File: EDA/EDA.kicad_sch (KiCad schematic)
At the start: 38 parts, among them J2 Screw_Terminal_01x02, M1 Motor_Servo, U1 PMCF8316A1VRGFR, U2 LM2596S-5, U3 LM2678S-5.0

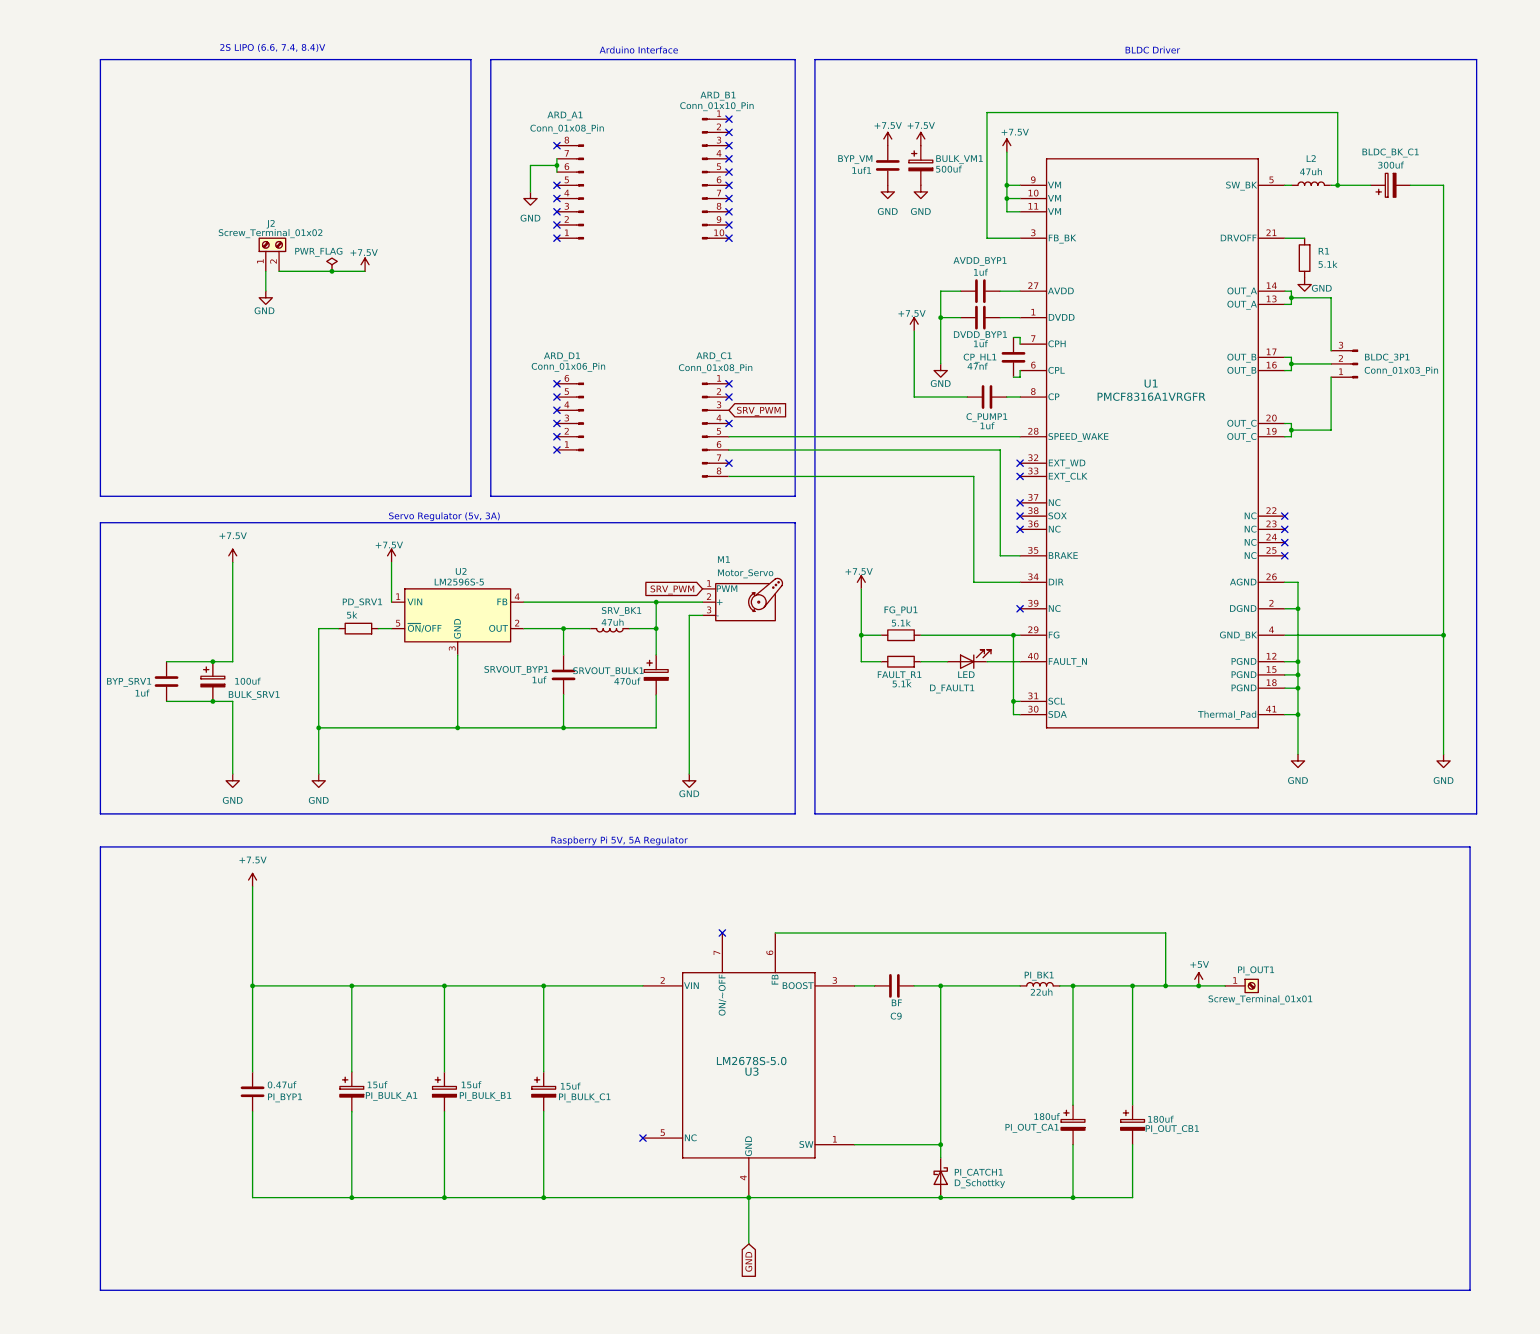
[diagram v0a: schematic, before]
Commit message: Add No-Connect flags and add labels, create ground terminal for Raspberry Pi.
Started Routing PCB.

- Developed Pi 5V, 5A power supply.
- Working on 5V, 3A servo power supply.
- Yet to begin wiring BLDC motor controller logic.
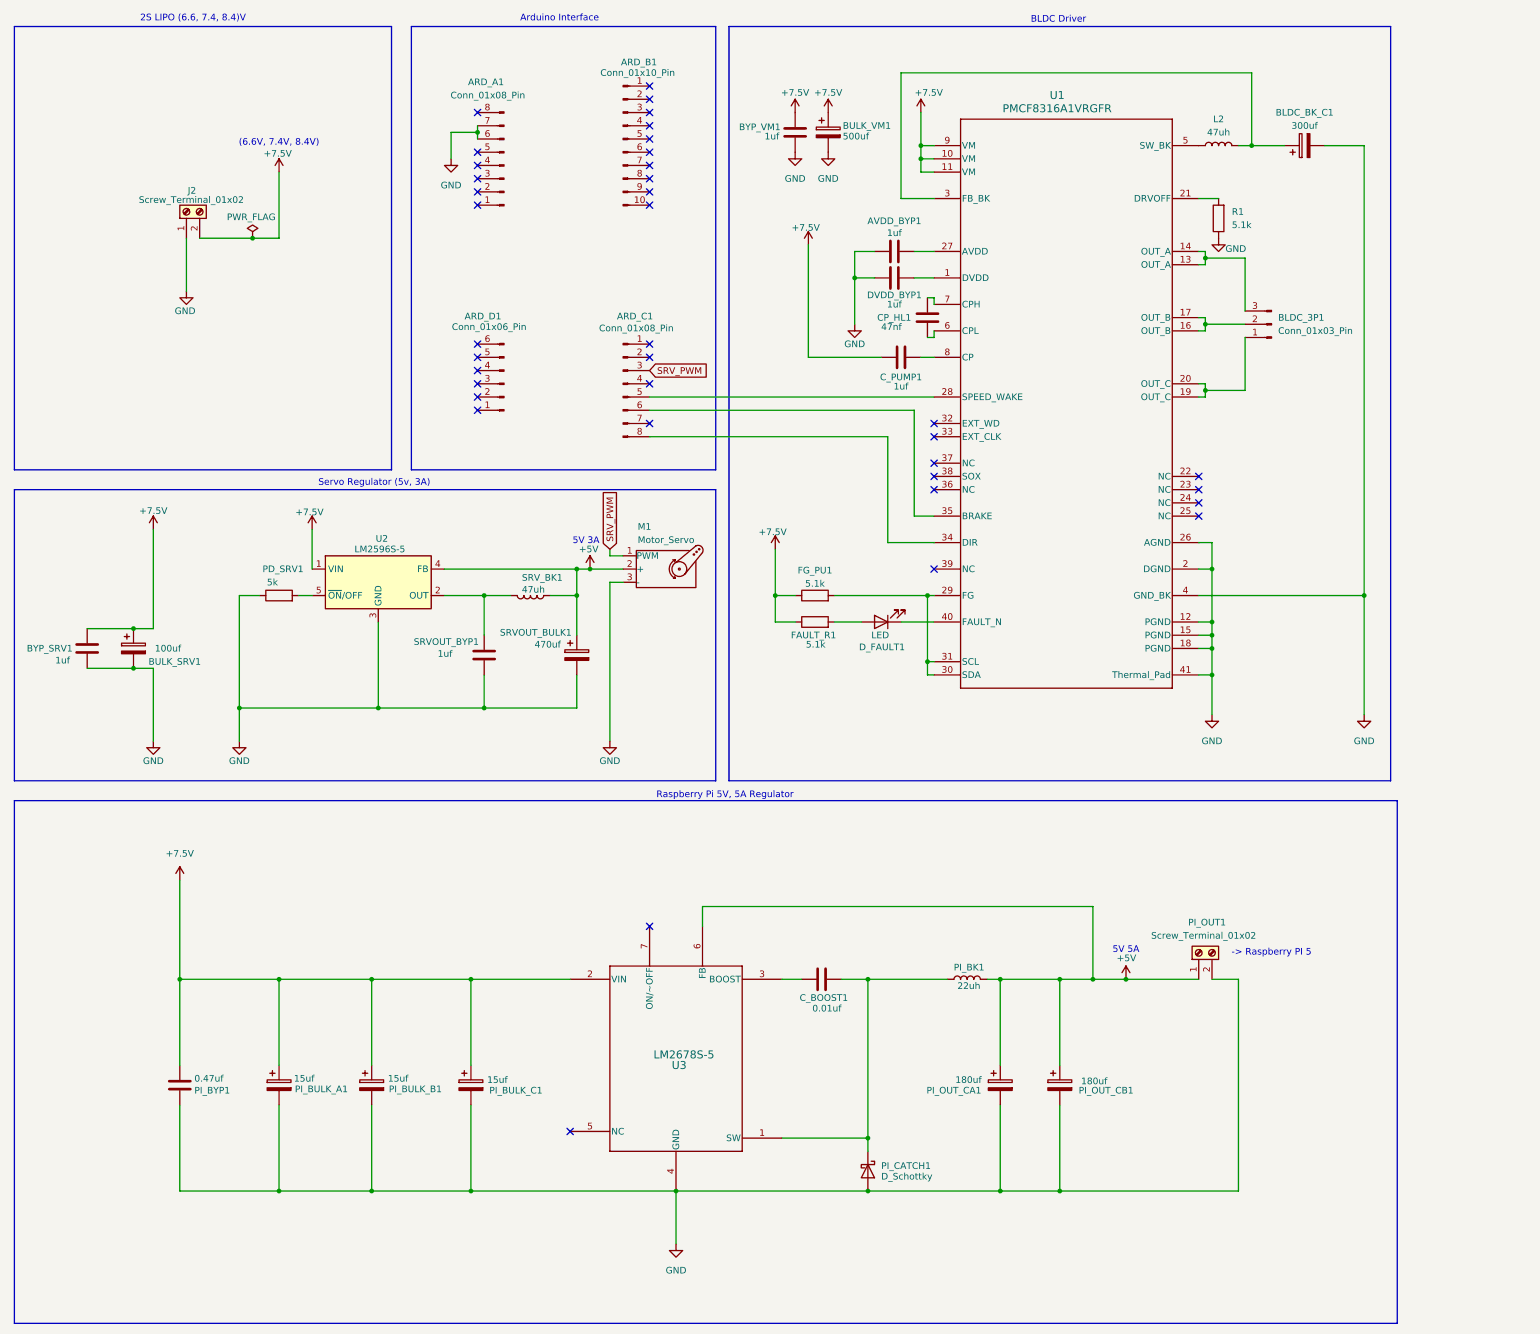
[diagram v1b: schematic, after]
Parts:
- removed PI_OUT1: Screw_Terminal_01x01, symbol Connector:Screw_Terminal_01x01
- added PI_OUT1: Screw_Terminal_01x02, Connector_Wire:SolderWire-1.5sqmm_1x02_P7.8mm_D1.7mm_OD3.9mm, symbol Connector:Screw_Terminal_01x02
- BLDC_BK_C1: footprint (none) -> Capacitor_THT:CP_Radial_D8.0mm_P3.50mm
- BULK_SRV1, PI_BULK_A1, PI_BULK_B1, PI_BULK_C1: footprint (none) -> Capacitor_THT:CP_Radial_D7.5mm_P2.50mm
- BYP_SRV1, PI_BYP1: footprint (none) -> Capacitor_SMD:C_0402_1005Metric
- BYP_VM1: renamed from 1uf1; value BYP_VM -> 1uf
- C_BOOST1: renamed from C9; value BF -> 0.01uf; footprint (none) -> Capacitor_SMD:C_0402_1005Metric
- PI_BK1: footprint (none) -> Inductor_SMD:L_0201_0603Metric
- PI_CATCH1: footprint (none) -> Diode_SMD:D_0201_0603Metric
- PI_OUT_CA1, PI_OUT_CB1: footprint (none) -> Capacitor_THT:CP_Radial_D8.0mm_P2.50mm
- SRVOUT_BULK1: footprint (none) -> Capacitor_THT:CP_Radial_D8.0mm_P3.80mm
- SRVOUT_BYP1: footprint (none) -> Capacitor_SMD:C_0201_0603Metric
- U3: value LM2678S-5.0 -> LM2678S-5
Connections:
- net +5V: now also M1.2 (+), SRVOUT_BULK1.1, SRV_BK1.1, U2.4 (FB), PI_OUT1.1 (Pin_1)
- net GND: now also PI_OUT1.2 (Pin_2)
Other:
- note added: "(6.6V, 7.4V, 8.4V)"
- note added: "-> Raspberry PI 5"
- note added: "5V 3A"
- note added: "5V 5A"
- company: (none) -> Apostla
- title: (none) -> BLDC Driver + Servo Shield + 5V, 5A Supply
- moved on the sheet: ARD_A1, ARD_B1, ARD_C1, ARD_D1, AVDD_BYP1, BLDC_3P1, BLDC_BK_C1, BULK_SRV1, BULK_VM1, BYP_SRV1, BYP_VM1, CP_HL1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

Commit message: Add initial EDA project files and configuration
- Created EDA.step file for project steps.
- Added autosave configuration for EDA.kicad_prl with board settings, visibility options, and net inspector panel configurations.
- Introduced lock files for PCB and schematic with hostname and username information.

Add components table to README

Added a table listing various components with their products and prices.

Add new symbols and footprints for UCY2D181MHD3TN and VS-6TQ045S-M3 components

- Created symbol for UCY2D181MHD3TN with properties including reference, value, footprint, and datasheet.
- Added footprint for UCY2D181MHD3TN with dimensions and pad specifications.
- Created symbol for VS-6TQ045S-M3 with properties including reference, value, footprint, and datasheet link.
- Added multiple footprints for VS-6TQ045S-M3, including DPAK_045S-M3_VIS, DPAK_045S-M3_VIS-L, and DPAK_045S-M3_VIS-M with detailed specifications.
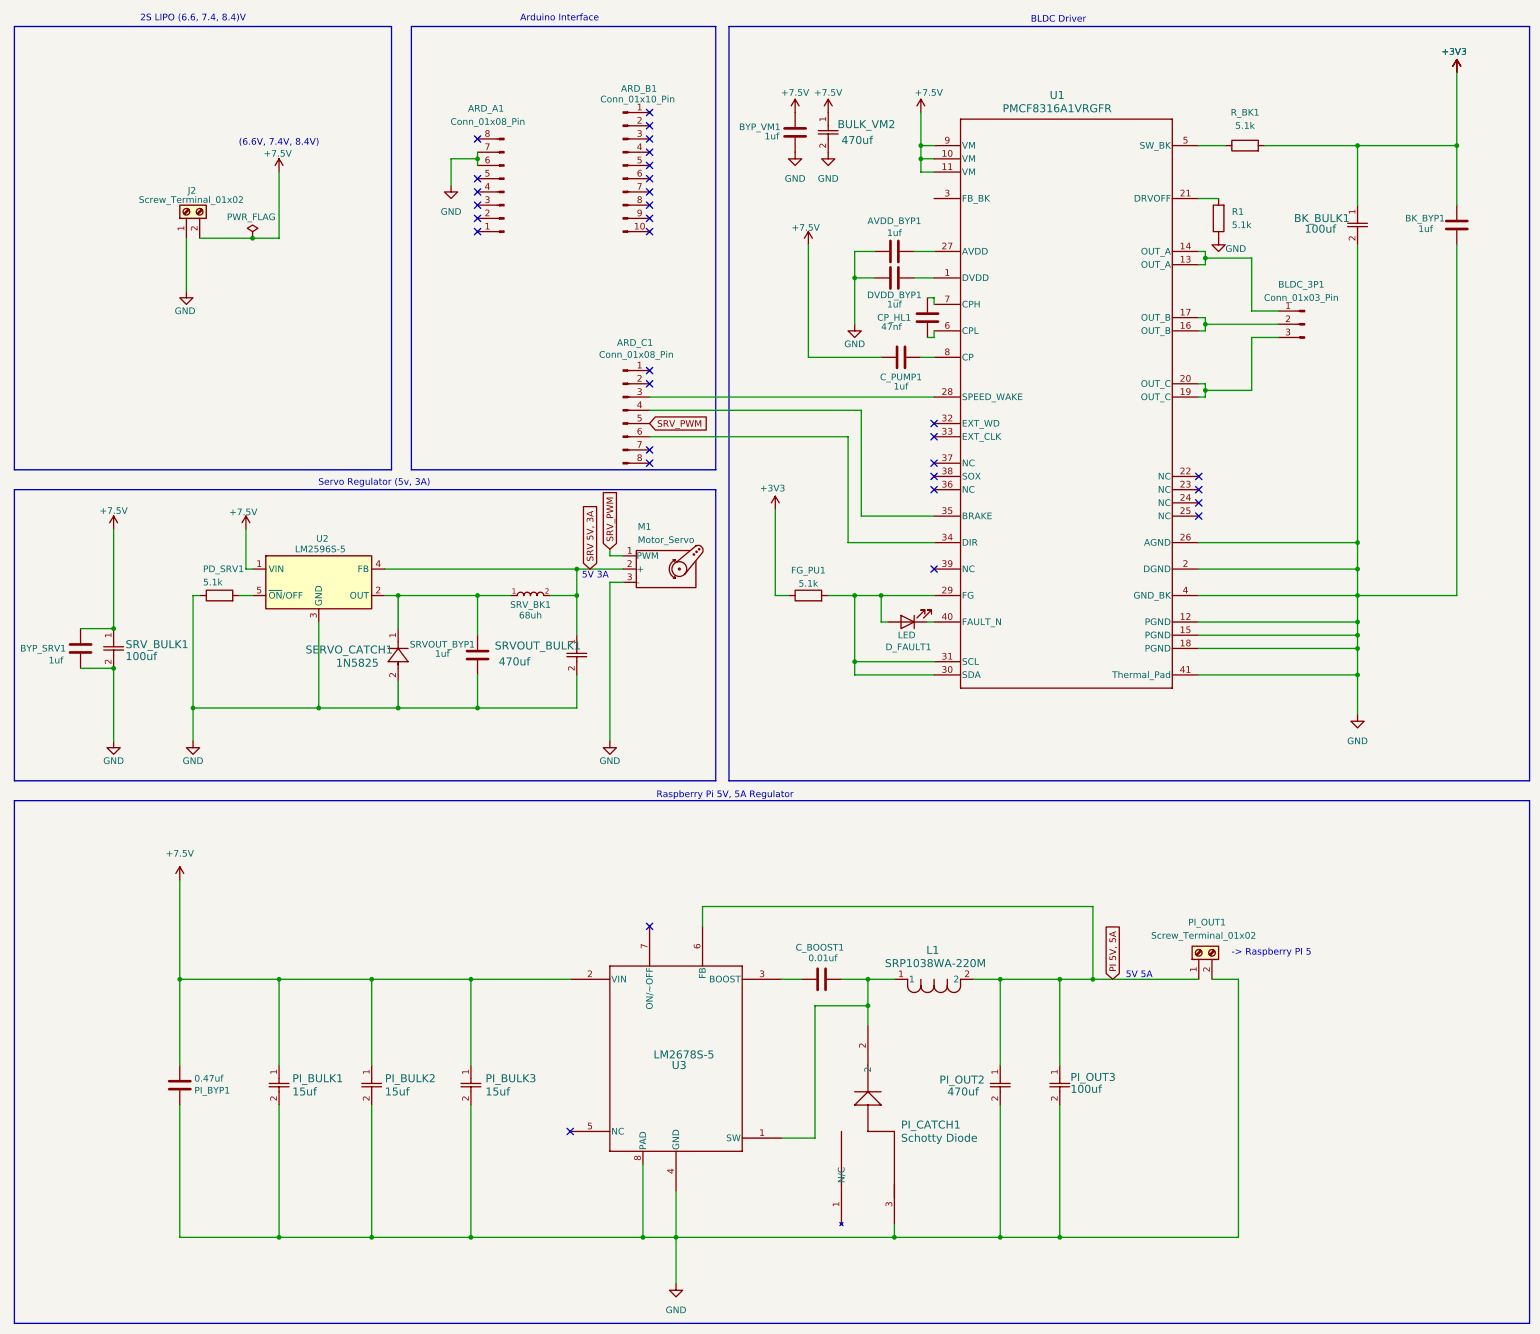
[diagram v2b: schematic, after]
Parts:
- removed ARD_D1: Conn_01x06_Pin, Connector_PinHeader_2.54mm:PinHeader_1x06_P2.54mm_Vertical, symbol Connector:Conn_01x06_Pin
- removed BLDC_BK_C1: 300uf, Capacitor_THT:CP_Radial_D8.0mm_P3.50mm, symbol Device:C_Polarized
- removed BULK_SRV1: 100uf, Capacitor_THT:CP_Radial_D7.5mm_P2.50mm, symbol Device:C_Polarized
- removed BULK_VM1: 500uf, Capacitor_THT:CP_Radial_D8.0mm_P3.50mm, symbol Device:C_Polarized
- removed FAULT_R1: 5.1k, Resistor_SMD:R_0402_1005Metric, symbol Device:R
- removed L2, SRV_BK1: 47uh, Inductor_SMD:L_0603_1608Metric, symbol Device:L
- removed PI_BK1: 22uh, Inductor_SMD:L_0201_0603Metric, symbol Device:L
- removed PI_BULK_A1, PI_BULK_B1, PI_BULK_C1: 15uf, Capacitor_THT:CP_Radial_D7.5mm_P2.50mm, symbol Device:C_Polarized
- removed PI_CATCH1: D_Schottky, Diode_SMD:D_0201_0603Metric, symbol Device:D_Schottky
- removed PI_OUT_CA1, PI_OUT_CB1: 180uf, Capacitor_THT:CP_Radial_D8.0mm_P2.50mm, symbol Device:C_Polarized
- removed SRVOUT_BULK1: 470uf, Capacitor_THT:CP_Radial_D8.0mm_P3.80mm, symbol Device:C_Polarized
- added BK_BULK1, PI_OUT3, SRV_BULK1: 100uf, 860040573004:CAP_WCAP-ATUL_06.3X11.0_WRE, symbol 860040573004:860040573004
- added BK_BYP1: 1uf, Capacitor_SMD:C_0201_0603Metric, symbol Device:C
- added BULK_VM2, PI_OUT2, SRVOUT_BULK1: 470uf, 16ZLH470MEFCT78X11.5:CAP_YX_8X11P5_RUB, symbol 16ZLH470MEFCT78X11.5:16ZLH470MEFCT78X11.5
- added L1: SRP1038WA-220M, SRP1038WA-220M:IND_SRP1038WA-220M_BRN, symbol SRP1038WA-220M:SRP1038WA-220M
- added PI_BULK1, PI_BULK2, PI_BULK3: 15uf, 860160572002:CAP_5X11_WRE, symbol 860160572002:860160572002
- added PI_CATCH1: Schotty Diode, VS-6TQ045S-M3:DPAK_045S-M3_VIS, symbol VS-6TQ045S-M3:VS-6TQ045S-M3
- added R_BK1: 5.1k, Resistor_SMD:R_0402_1005Metric, symbol Device:R
- added SERVO_CATCH1: 1N5825, 1N5825:1N5825_MCH, symbol 1N5825:1N5825
- added SRV_BK1: 68uh, SPM10065VT-680M-D:IND_SPM10065VT-680M-D, symbol SPM10065VT-680M-D:SPM10065VT-680M-D
- BLDC_3P1: footprint Connector_JST:JST_PH_B3B-PH-K_1x03_P2.00mm_Vertical -> Connector_JST:JST_PH_S3B-PH-K_1x03_P2.00mm_Horizontal
- M1: footprint Connector_PinHeader_2.54mm:PinHeader_1x03_P2.54mm_Vertical -> Connector_PinHeader_2.54mm:PinHeader_1x03_P2.54mm_Horizontal
- PD_SRV1: value 5k -> 5.1k
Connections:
- net +7.5V: now also BULK_VM2.1, PI_BULK1.1, PI_BULK2.1, PI_BULK3.1, SRV_BULK1.1; no longer FG_PU1.1
- net GND: now also U3.8 (PAD), BK_BULK1.2, BK_BYP1.2, BULK_VM2.2, PI_BULK1.2, PI_BULK2.2, PI_BULK3.2, PI_CATCH1.3, PI_OUT2.2, PI_OUT3.2, SERVO_CATCH1.2, SRVOUT_BULK1.2, SRV_BULK1.2
- net SRV_PWM: now also ARD_C1.5 (Pin_5); no longer ARD_C1.3 (Pin_3)
- net at FG_PU1.2, U1.29 (FG), U1.30 (SDA)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: now also D_FAULT1.2 (A)
- net at SRVOUT_BYP1.1, U2.2 (OUT): now also SERVO_CATCH1.1, SRV_BK1.1
- net at ARD_C1.4 (Pin_4): now also U1.35 (BRAKE)
- net at U1.28 (SPEED_WAKE): now also ARD_C1.3 (Pin_3); no longer ARD_C1.5 (Pin_5)
- net at ARD_C1.6 (Pin_6): now also U1.34 (DIR); no longer U1.35 (BRAKE)
- net at ARD_C1.8 (Pin_8): no longer U1.34 (DIR)
- net at U1.13 (OUT_A), U1.14 (OUT_A): now also BLDC_3P1.1 (Pin_1); no longer BLDC_3P1.3 (Pin_3)
- net at U1.19 (OUT_C), U1.20 (OUT_C): now also BLDC_3P1.3 (Pin_3); no longer BLDC_3P1.1 (Pin_1)
- net at U1.5 (SW_BK): now also R_BK1.1
- net at C_BOOST1.2, U3.1 (SW): now also L1.1, PI_CATCH1.2
- net +5V renamed PI 5V, 5A
- net PI 5V, 5A: now also L1.2, PI_OUT2.1, PI_OUT3.1; no longer M1.2 (+), U2.4 (FB)
- new net +3V3: BK_BULK1.1, BK_BYP1.1, FG_PU1.1, R_BK1.2
- new net SRV 5V, 3A: M1.2 (+), SRVOUT_BULK1.1, SRV_BK1.2, U2.4 (FB)
- no-connect marks 38 -> 32
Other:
- moved on the sheet: ARD_A1, ARD_B1, ARD_C1, BLDC_3P1, BYP_SRV1, D_FAULT1, FG_PU1, PD_SRV1, SRVOUT_BYP1, U2
